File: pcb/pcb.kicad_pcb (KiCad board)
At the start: 2 copper layers, 149.6 x 79.8 mm, 51 parts, among them J1 Ribbon Cable Header, J2 Ribbon Cable Header, J3 ISP, SW1 MX Grey w/ LED, SW2 MX Grey w/ LED, SW3 1241.1100.7095, SW4 SW_SPST, U1 Display Driver, U2 Display Driver, U3 MCU, U4 Inverter, 3 Channels, U5 3:8 Demux, U6 NOR, 4 Channels, U7 OR, 2 Channels, U8 5V Buck Voltage Regulator, Y1 20MHz

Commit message: Add some models
Signed-off-by: Michael Darr <michael.e.darr@gmail.com>
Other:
- outline, holes or cut-outs redrawn
- board text added: "0.1.0"
- board text added: "OH NO"
- board text added: "┏━⬓━━▬━━⬓━. ┌──┚`▝███▖▜██▙`ˎ─. │╲ ꞌ━━━━━━━━━┙ ╲ │ ╒═════╤══════════╕ │╲│ REV │ 0.1.0 │ │ ├─────┼──────────┤ ╵╲│ MFR │ JLCPCB │ ├─────┴──────────┤"
- board text added: "╔════════╗ ║ ║ ╚════════╝"
- board text added: "♜ ♝ ♛ ♞ ♜ ♟ ♟ ♗ ♚ ♟ ♟ ♟ ♟ ♗ ♘ ♙ ♙ ♙ ♙ ♙ ♙ ♙ ♖ ♔ ♝ ♖"
- board text removed: "╔════════╗ ║ ║ ╚════════╝ ┏━⬓━━▬━━⬓━. ┌──┚`▝███▖▜██▙`ˎ─. │╲ ꞌ━━━━━━━━━┙ ╲ │ ╒═════╤══════════╕ │╲│ REV │ 0.1.0 │ │ ├─────┼──────────┤ ╵╲│ MFR │ JLCPCB │ ├─────┴──────────┤"

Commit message: standardize cross-connector net names
Signed-off-by: Michael Darr <michael.e.darr@gmail.com>
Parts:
- removed the C10 at (127.0, 66.0)
- removed C14: 22pF, Capacitor_SMD:C_0805_2012Metric_Pad1.18x1.45mm_HandSolder
- removed C15: 0.1µF, Capacitor_SMD:C_0805_2012Metric_Pad1.18x1.45mm_HandSolder
- removed D2: TVS Diode, Diode_SMD:D_SOD-523
- removed FET1, FET2: PMOS, Package_TO_SOT_THT:TO-220-3_Vertical
- removed R10: 4.7kΩ, Resistor_SMD:R_0805_2012Metric_Pad1.20x1.40mm_HandSolder
- removed R5: 5.6kΩ, Resistor_SMD:R_0805_2012Metric_Pad1.20x1.40mm_HandSolder
- removed R6, R7, R8: 100kΩ, Resistor_SMD:R_0805_2012Metric_Pad1.20x1.40mm_HandSolder
- removed R9: 50Ω, chess_clock:352151RFT
- removed U6: NOR, 4 Channels, chess_clock:SN74F02D
- removed U7: OR, 2 Channels, chess_clock:TC7WZ32FK_LJCT
- removed U8: 5V Buck Voltage Regulator, chess_clock:MAX5035BUSA+
- C10: renamed from C11; value 0.1µF -> 10nF
- C11: renamed from C12; value 68µF -> 22pF; footprint chess_clock:TPSD686K010R0100 -> Capacitor_SMD:C_0805_2012Metric_Pad1.18x1.45mm_HandSolder
- C8: value 0.1µF -> 68µF; footprint Capacitor_SMD:C_0805_2012Metric_Pad1.18x1.45mm_HandSolder -> chess_clock:TPSD686K010R0100
- J3: value ISP -> UPDI
- R4: value 4.7kΩ -> 50Ω; footprint Resistor_SMD:R_0805_2012Metric_Pad1.20x1.40mm_HandSolder -> chess_clock:352151RFT
- U3: footprint chess_clock:ATtiny84a -> chess_clock:ATTINY1627
- U4: value Inverter, 3 Channels -> OR, 2 Channels; footprint chess_clock:NL37WZ14USG -> chess_clock:TC7WZ32FK_LJCT
- U5: value 3:8 Demux -> 5V Buck Voltage Regulator; footprint chess_clock:SN74AHC138DR -> chess_clock:MAX5035BUSA+
- Y1: value 20MHz -> 32.768 kHz; footprint chess_clock:ABM8-20.000MHZ-10-B1U-T -> chess_clock:CM315D32768HZFT
- moved LS1 52.5 mm to (148.8, 115.0), turned to 90 degrees
- moved J3 45.7 mm to (116.0, 89.9), turned to 90 degrees
- moved C9 42.6 mm to (187.8, 77.2)
- moved D1 42.6 mm to (179.6, 77.7)
- moved C4 32.0 mm to (162.9, 101.0), turned to 0 degrees
- moved R4 30.6 mm to (114.1, 83.2)
- moved U4 27.0 mm to (163.4, 98.3), turned to 180 degrees
- moved C10 22.0 mm to (139.1, 86.4)
- moved C8 17.6 mm to (117.5, 78.4), turned to 0 degrees
- moved C11 14.8 mm to (129.4, 78.0), turned to -45 degrees
- moved R3 12.0 mm to (90.2, 74.8), turned to 0 degrees
- moved C5 11.5 mm to (172.3, 78.2)
- moved C3 11.3 mm to (136.9, 86.4), turned to 90 degrees
- moved SW4 11.2 mm to (123.2, 75.0)
- moved BT1 11.0 mm to (76.7, 75.0)
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- renumbered C13 to C12
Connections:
- net cs_1_1 renamed LATCH_1
- net cs_1_2 renamed LATCH_2
- net cs_2 renamed WRITE
- net d0 renamed DATA0
- net d1 renamed DATA1
- net d2 renamed DATA2
- net d3 renamed DATA3
- net data_0 renamed LCD_DATA0
- net data_1 renamed LCD_DATA1
- net ds_1 renamed DIGIT1
- net ds_2 renamed DIGIT2
- C10 pad 1: GND -> VCC
- C10 pad 2: Net-(U8-VD) -> GND
- C11 pad 1: VCC -> GND
- C11 pad 2: GND -> Net-(U3-PB3(TOSC1))
- C12 pad 2: Net-(U3-(PCINT8/XTAL1/CLKI)_PB0) -> Net-(U3-PB2(TOSC2))
- C4 pad 1: VCC -> VDD
- C4 pad 2: GND -> VSS
- C5 pad 1: VCC -> Net-(D1-K)
- C5 pad 2: GND -> Net-(U5-BST)
- C6 pad 1: VCC -> VBAT_PROT
- C7 pad 1: VCC -> GND
- C7 pad 2: GND -> Net-(U5-VD)
- C8 pad 1: Net-(D1-K) -> VCC
- C8 pad 2: Net-(U8-BST) -> GND
- C9 pad 1: Net-(U8-VIN) -> VBAT_PROT
- J1 pad 1: col1_bp -> LCD_BUZZ
- J1 pad 11: lcd_bp -> LCD_COL_1
- J1 pad 12: lcd2_write -> LCD_LATCH_2
- J1 pad 14: ~{lcd_bp} -> LCD_COL_2
- J1 pad 3: mux_b -> LCD_WRITE
- J1 pad 4: lcd1_write -> LCD_LATCH_1
- J1 pad 5: digit_2 -> LCD_DIGIT2
- J1 pad 6: digit_1 -> LCD_DIGIT1
- J1 pad 7: data_3 -> LCD_DATA3
- J1 pad 8: data_2 -> LCD_DATA2
- J2 pad 1: col1 -> /BUZZ
- J2 pad 11: bp -> COL_1
- J2 pad 14: ~{bp} -> COL_2
- J3 pad 1: digit_1 -> UDPI
- J3 pad 3: digit_2 -> unconnected-(J3-Pin_3-Pad3)
- J3 pad 4: data_2 -> unconnected-(J3-Pin_4-Pad4)
- J3 pad 5: ~{col1_enable} -> unconnected-(J3-Pin_5-Pad5)
- LCD1 pad 1: bp -> BP
- LCD1 pad 12: bp -> BP
- LCD1 pad 16: bp -> BP
- LCD1 pad 28: col1 -> COL_BP_1
- LCD1 pad 40: bp -> BP
- LCD1 pad 8: bp -> BP
- LCD2 pad 1: bp -> BP
- LCD2 pad 12: bp -> BP
- LCD2 pad 16: bp -> BP
- LCD2 pad 28: ~{bp} -> COL_BP_2
- LCD2 pad 40: bp -> BP
- LCD2 pad 8: bp -> BP
- LED1 pad 1: Net-(LED1-K) -> GND
- LED1 pad 2: Net-(FET1-D) -> Net-(LED1-A)
- LS1 pad 1: /buzz -> /BUZZ
- LS1 pad 2: GND -> VSS
- R1 pad 1: /led_1 -> /SW1_LED_ENABLE
- R2 pad 1: /led_2 -> /SW2_LED_ENABLE
- R3 pad 1: Net-(BT1--) -> Net-(LED1-A)
- R3 pad 2: Net-(LED1-K) -> /LED1_ENABLE
- R4 pad 1: Net-(FET1-G) -> Net-(BT1-+)
- R4 pad 2: Net-(BT1-+) -> VBAT_PROT
- SW1 pad 2: Net-(R6-Pad1) -> /~{SW1_ACTIVE}
- SW2 pad 1: Net-(R7-Pad1) -> GND
- SW2 pad 2: GND -> /~{SW2_ACTIVE}
- SW3 pad 1: Net-(R8-Pad1) -> GND
- SW3 pad 2: GND -> /~{SW3_ACTIVE}
- U1 pad 5: bp -> BP
- U2 pad 5: bp -> BP
- U3 pad 1: VCC -> LCD_LATCH_1
- U3 pad 10: data_3 -> LCD_DIGIT1
- U3 pad 11: mux_b -> LCD_COL_2
- U3 pad 12: /mux_a -> LCD_COL_1
- U3 pad 13: mux_c -> Net-(U3-PB3(TOSC1))
- U3 pad 14: GND -> Net-(U3-PB2(TOSC2))
- U3 pad 2: Net-(U3-(PCINT8/XTAL1/CLKI)_PB0) -> LCD_LATCH_2
- U3 pad 3: Net-(U3-(PCINT9/XTAL2)_PB1) -> GND
- U3 pad 4: ~{col1_enable} -> VCC
- U3 pad 7: data_2 -> LCD_DATA2
- U3 pad 8: digit_2 -> LCD_DATA3
- U3 pad 9: digit_1 -> LCD_DIGIT2
- U4 pad 1: ~{led_1} -> BP
- U4 pad 2: ~{lcd_bp} -> COL_2
- U4 pad 3: ~{led_2} -> COL_BP_1
- U4 pad 4: GND -> VSS
- U4 pad 5: /led_2 -> COL_1
- U4 pad 6: lcd_bp -> BP
- U4 pad 7: /led_1 -> COL_BP_2
- U4 pad 8: VCC -> VDD
- U5 pad 1: /mux_a -> Net-(U5-BST)
- U5 pad 2: mux_b -> Net-(U5-VD)
- U5 pad 3: mux_c -> GND
- U5 pad 4: GND -> VCC
- U5 pad 6: VCC -> GND
- U5 pad 7: ~{sw3_enable} -> VBAT_PROT
- U5 pad 8: GND -> Net-(D1-K)
- Y1 pad 1: Net-(U3-(PCINT9/XTAL2)_PB1) -> Net-(U3-PB2(TOSC2))
- Y1 pad 2: GND -> Net-(U3-PB3(TOSC1))
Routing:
- net bp: track 421.0 -> 0.00 mm
- net BP: track 0.00 -> 417.5 mm, vias 0 -> 1
- net VCC: track 276.2 -> 118.5 mm, vias 9 -> 3
- net /led_1: track 120.2 -> 0.00 mm
- net data_3: track 119.2 -> 0.00 mm
- net VBAT_PROT: track 0.00 -> 107.6 mm, vias 0 -> 4
- net ~{col1_enable}: track 106.4 -> 0.00 mm, vias 2 -> 0
- net /~{SW2_ACTIVE}: track 0.00 -> 96.7 mm, vias 0 -> 1
- net digit_1: track 83.3 -> 0.00 mm, vias 1 -> 0
- net /SW2_LED_ENABLE: track 0.00 -> 78.9 mm, vias 0 -> 2
- net data_2: track 72.6 -> 0.00 mm, vias 1 -> 0
- net digit_2: track 69.3 -> 0.00 mm, vias 1 -> 0
- net COL_BP_1: track 0.00 -> 68.1 mm, vias 0 -> 1
- net GND: track 91.8 -> 156.7 mm, vias 247 -> 160
- net LCD_LATCH_1: track 0.00 -> 63.5 mm
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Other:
- board size 149.6 x 79.8 mm -> 149.6 x 68.5 mm
- board text added: "0.2.0"
- board text added: "┏━⬓━━▬━━⬓━. ┌──┚`▝███▖▜██▙`ˎ─. │╲ ꞌ━━━━━━━━━┙ ╲ │ ╒═════╤══════════╕ │╲│ REV │ 0.2.0 │ │ ├─────┼──────────┤ ╵╲│ MFR │ JLCPCB │ ├─────┴──────────┤"
- board text removed: "0.1.0"
- board text removed: "OH NO"
- board text removed: "┏━⬓━━▬━━⬓━. ┌──┚`▝███▖▜██▙`ˎ─. │╲ ꞌ━━━━━━━━━┙ ╲ │ ╒═════╤══════════╕ │╲│ REV │ 0.1.0 │ │ ├─────┼──────────┤ ╵╲│ MFR │ JLCPCB │ ├─────┴──────────┤"
- board text removed: "♜ ♝ ♛ ♞ ♜ ♟ ♟ ♗ ♚ ♟ ♟ ♟ ♟ ♗ ♘ ♙ ♙ ♙ ♙ ♙ ♙ ♙ ♖ ♔ ♝ ♖"

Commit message: 0.2.0
Signed-off-by: Michael Darr <michael.e.darr@gmail.com>
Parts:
- removed the C5 at (172.3, 78.2)
- removed the C9 at (187.8, 77.2)
- BT1: footprint Connector_Wire:SolderWire-0.15sqmm_1x02_P4mm_D0.5mm_OD1.5mm -> chess_clock:BATTERY
- C7: value 0.1µF -> 10µF
- U5: value 5V Buck Voltage Regulator -> Voltage Regulator; footprint chess_clock:MAX5035BUSA+ -> chess_clock:MAX1836EUT50+T
- moved BT1 73.2 mm to (149.7, 79.8), turned to -90 degrees
- moved D1 66.6 mm to (113.2, 81.8)
- moved C5 61.2 mm to (109.5, 89.8), turned to 0 degrees
- moved C7 59.2 mm to (115.3, 77.8), turned to -90 degrees
- moved SW4 55.1 mm to (178.0, 80.6)
- moved U5 52.3 mm to (111.9, 77.7), turned to 180 degrees
- moved R4 23.2 mm to (136.6, 77.3), turned to 180 degrees
- moved R1 11.0 mm to (92.3, 89.8)
- moved LED1 9.66 mm to (92.0, 82.6), turned to 90 degrees
- moved C6 8.92 mm to (113.3, 86.2)
- moved J3 5.79 mm to (121.8, 90.3)
- moved R3 4.50 mm to (92.0, 78.9), turned to 90 degrees
- moved SW3 3.81 mm to (149.6, 82.7)
- moved SW1 1.80 mm to (82.9, 83.0)
- moved SW2 1.80 mm to (216.0, 83.0)
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- renumbered C12 to C10, C6 to C5, C8 to C6, C10 to C8, C11 to C9
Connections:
- C5 pad 1: VBAT_PROT -> VCC
- C7 pad 1: GND -> VBAT_PROT
- C7 pad 2: Net-(U5-VD) -> GND
- J1 pad 1: LCD_BUZZ -> LCD_COL_2
- J1 pad 10: LCD_DATA0 -> LCD_DIGIT2
- J1 pad 11: LCD_COL_1 -> LCD_LATCH_1
- J1 pad 12: LCD_LATCH_2 -> LCD_WRITE
- J1 pad 13: GND -> VCC
- J1 pad 14: LCD_COL_2 -> LCD_BUZZ
- J1 pad 2: VCC -> GND
- J1 pad 3: LCD_WRITE -> LCD_LATCH_2
- J1 pad 4: LCD_LATCH_1 -> LCD_COL_1
- J1 pad 5: LCD_DIGIT2 -> LCD_DATA0
- J1 pad 6: LCD_DIGIT1 -> LCD_DATA1
- J1 pad 7: LCD_DATA3 -> LCD_DATA2
- J1 pad 8: LCD_DATA2 -> LCD_DATA3
- J1 pad 9: LCD_DATA1 -> LCD_DIGIT1
- U5 pad 1: Net-(U5-BST) -> GND
- U5 pad 2: Net-(U5-VD) -> GND
- U5 pad 3: GND -> VBAT_PROT
- U5 pad 4: VCC -> Net-(D1-K)
- U5 pad 5: GND -> VBAT_PROT
- U5 pad 6: GND -> VCC
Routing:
- net GND: track 156.7 -> 13.5 mm, vias 160 -> 171
- net Net-(D1-K): track 142.3 -> 9.76 mm
- net VBAT_PROT: track 107.6 -> 43.2 mm
- net LCD_DATA0: track 67.8 -> 40.7 mm, vias 0 -> 2
- net Net-(BT1-+): track 37.8 -> 12.3 mm
- net LCD_DATA1: track 60.6 -> 43.8 mm, vias 1 -> 2
- net Net-(U5-VD): track 16.1 -> 0.00 mm
- net /SW1_LED_ENABLE: track 43.2 -> 56.6 mm, vias 2 -> 0
- net LCD_LATCH_2: track 47.0 -> 33.7 mm
- net Net-(U5-BST): track 12.3 -> 0.00 mm
- net Net-(BT1--): track 29.3 -> 18.3 mm
- net UDPI: track 21.0 -> 14.9 mm
- net Net-(SW1-A): track 14.0 -> 9.25 mm
- net /~{SW1_ACTIVE}: track 51.2 -> 53.9 mm
- net LCD_DATA3: track 51.5 -> 54.0 mm
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- added copper zone on F.Cu, net VCC
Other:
- board size 149.6 x 68.5 mm -> 149.6 x 66.4 mm
- rule pad_to_mask_clearance: 0.038 -> 0

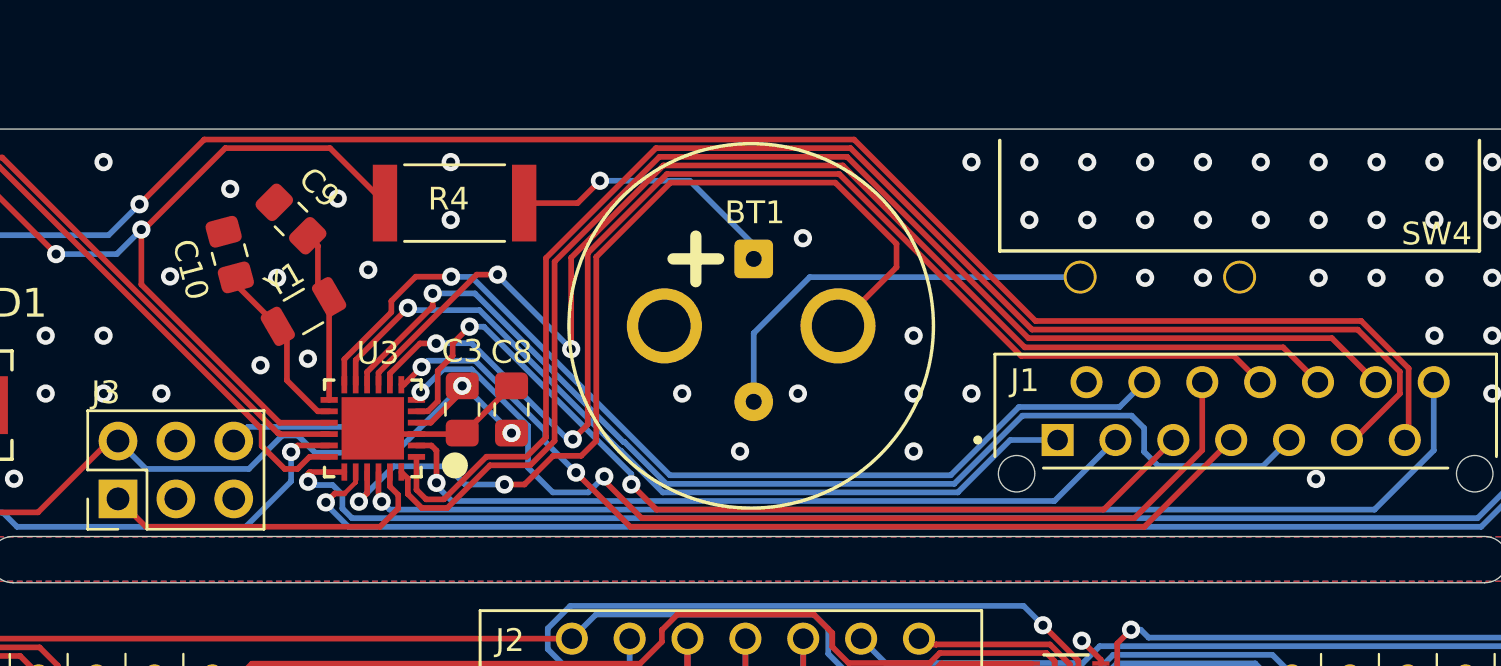
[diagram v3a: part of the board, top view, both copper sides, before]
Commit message: Update mcs 18 front footprint
Signed-off-by: Michael Darr <michael.e.darr@gmail.com>
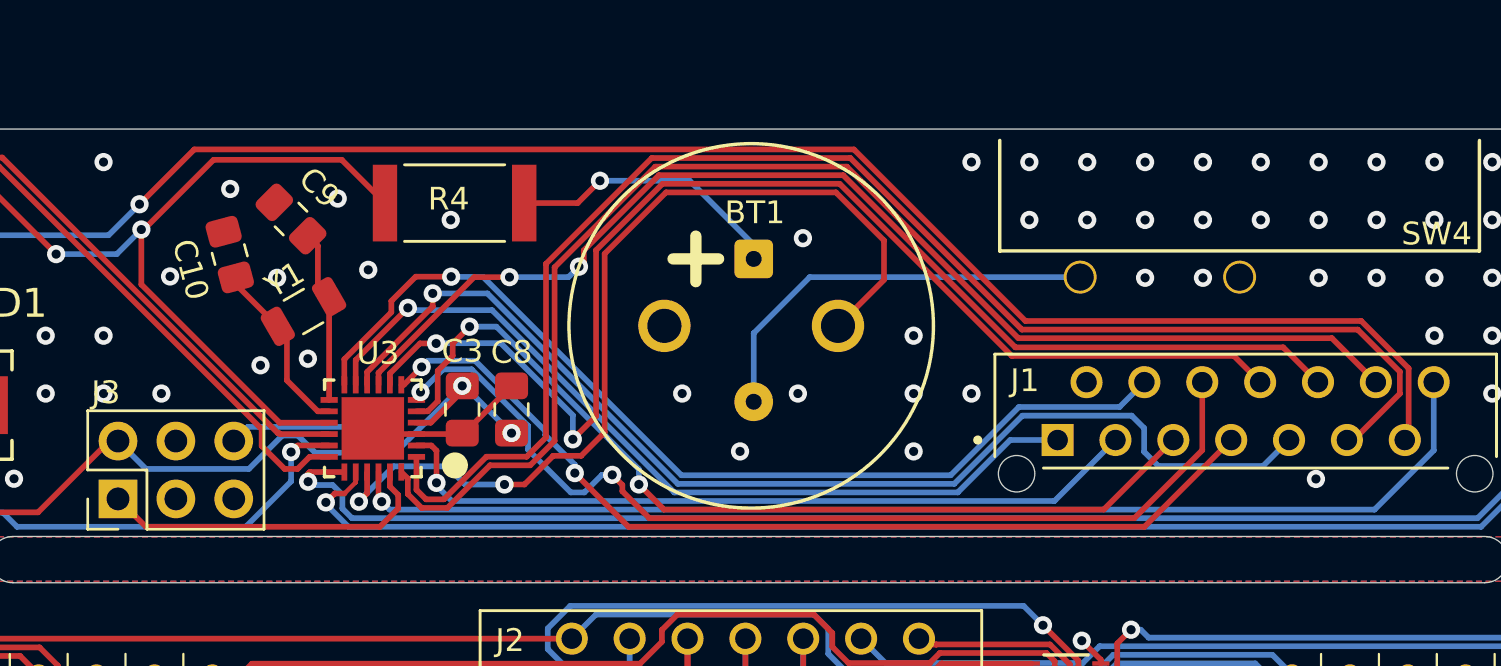
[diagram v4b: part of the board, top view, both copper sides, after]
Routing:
- net LCD_DIGIT2: track 54.6 -> 49.4 mm
- net /~{SW3_ACTIVE}: track 42.0 -> 40.8 mm
- net LCD_LATCH_1: track 64.0 -> 63.5 mm
- net LCD_WRITE: track 58.9 -> 58.4 mm
- net GND: vias 171 -> 170
